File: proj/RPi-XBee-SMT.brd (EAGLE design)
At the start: 49.5 x 49.5 mm, 32 parts, among them IC1 LM1117-3.3, Q1 BSN20, Q2 BSN20, Q3 BSN20, U1 QUBIQ_XBEE-SMT, U2 XBEE-1B1

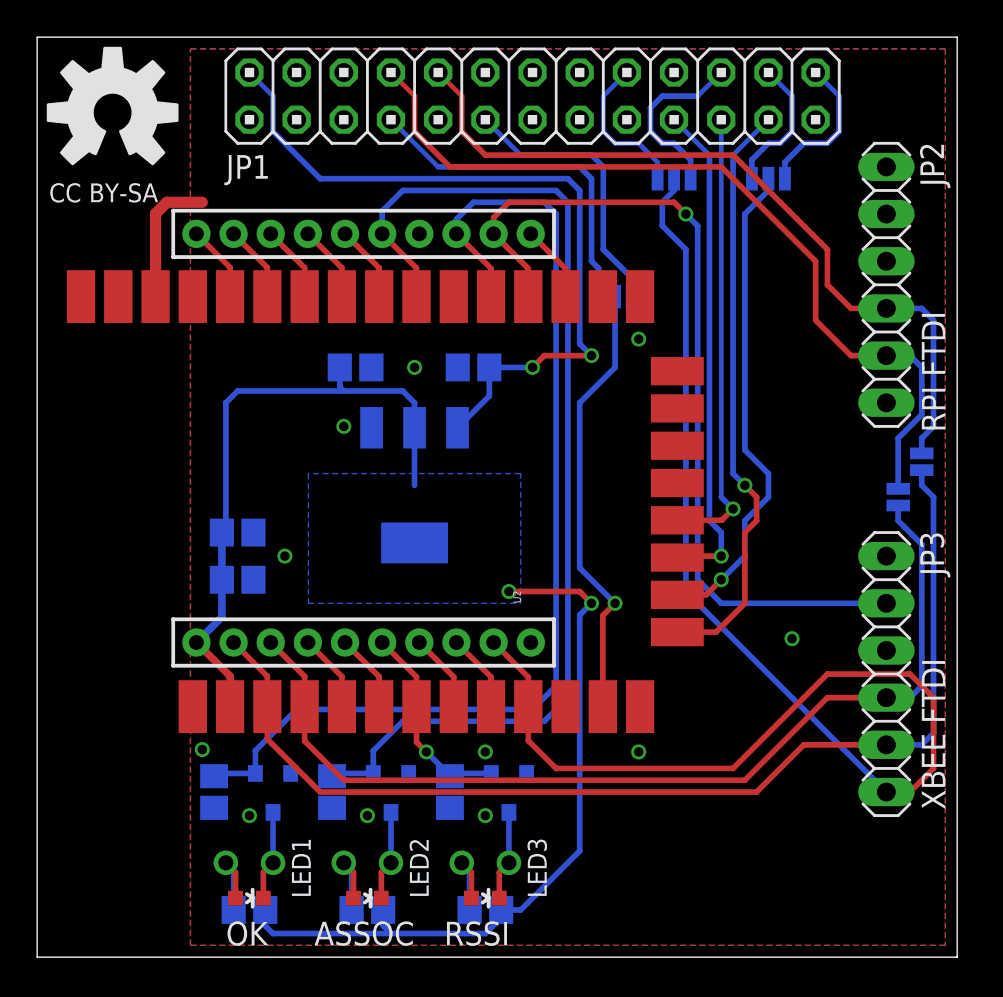
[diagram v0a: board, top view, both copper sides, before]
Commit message: Add solder jumper to power XBee from RPI 3.3V
This will allow people to omit the LDO if they would rather power the
XBee module straight from the Raspberry Pi's 3.3V rail.

This update also does some minor trace re-routing and moves some text
around the board a bit.
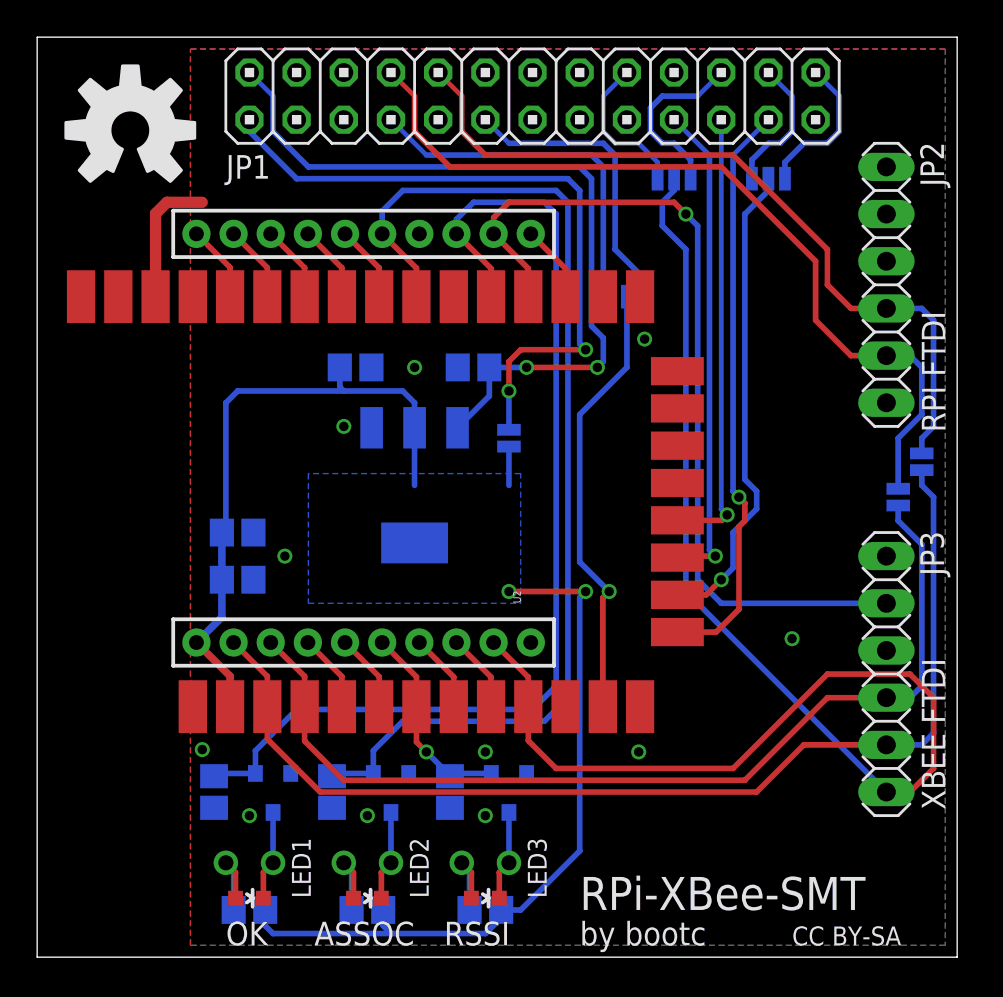
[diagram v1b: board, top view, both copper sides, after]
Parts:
- added SJ6: SOLDERJUMPERNO, SparkFun-Passives:SJ_2S-NO
- moved U$4 1.35 mm to (5.02, 44.5)
- moved SJ4 0.64 mm to (31.8, 35.6)
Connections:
- removed net 3V3: JP1.1
- new net RPI_3.3V: JP1.1, SJ6.2
- net 3.3V: now also SJ6.1
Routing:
- net RPI_3.3V: track 0.00 -> 36.5 mm, vias 0 -> 2
- net 3.3V: track 74.0 -> 76.1 mm
- net 5V: track 40.4 -> 42.2 mm
- net RPI_GPIO17: track 15.0 -> 16.0 mm
- net RPI_GPIO4: track 18.6 -> 19.6 mm
- net SCLK: track 31.9 -> 31.4 mm
- net ZB_!CSEL: track 26.4 -> 25.9 mm
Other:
- board text added: "RPi-XBee-SMT"
- board text added: "by bootc"
- board text removed: "SJ1"
- board text removed: "SJ2&3"
- board text removed: "SJ4"
- board text removed: "SJ5"
